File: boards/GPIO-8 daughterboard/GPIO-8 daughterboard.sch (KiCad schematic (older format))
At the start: 1 part, among them P0 HEADER

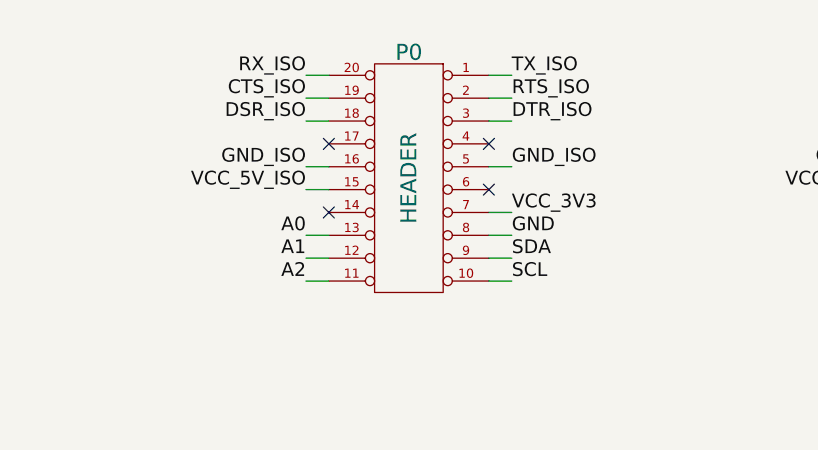
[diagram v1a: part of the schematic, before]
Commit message: Updated daughterboard header pinout in all sheets to be PMOD UART 4/4A compatible
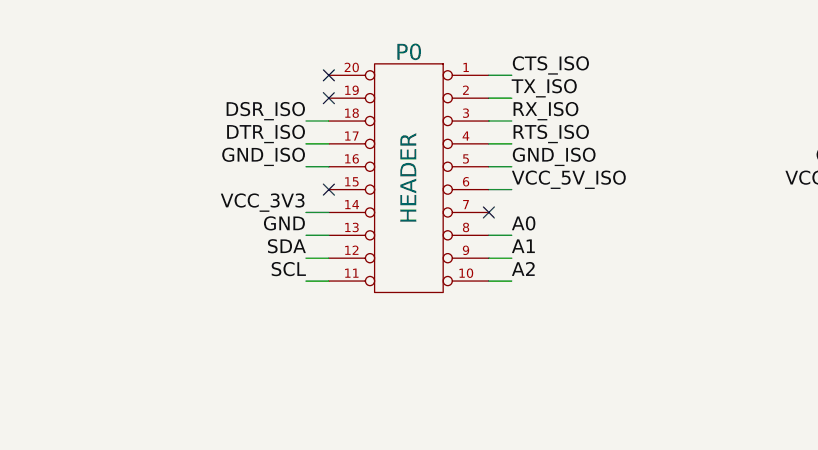
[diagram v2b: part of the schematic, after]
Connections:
- net A0: now also P0.8 (P8); no longer P0.13 (P13)
- net A1: now also P0.9 (P9); no longer P0.12 (P12)
- net A2: now also P0.10 (P10); no longer P0.11 (P11)
- net CTS_ISO: now also P0.1 (P1); no longer P0.19 (P19)
- net DTR_ISO: now also P0.17 (P17); no longer P0.3 (P3)
- net GND: now also P0.13 (P13); no longer P0.8 (P8)
- net RTS_ISO: now also P0.4 (P4); no longer P0.2 (P2)
- net RX_ISO: now also P0.3 (P3); no longer P0.20 (P20)
- net SCL: now also P0.11 (P11); no longer P0.10 (P10)
- net SDA: now also P0.12 (P12); no longer P0.9 (P9)
- net TX_ISO: now also P0.2 (P2); no longer P0.1 (P1)
- net VCC_3V3: now also P0.14 (P14); no longer P0.7 (P7)
- net VCC_5V_ISO: now also P0.6 (P6); no longer P0.15 (P15)
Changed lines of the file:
@@
 Sheet 1 3
 Title ""
-Date "26 jun 2014"
+Date "1 jul 2014"
 Rev ""
 Comp ""
@@
 $EndSheet
 Wire Wire Line
-	3750 3250 3650 3250
+	3750 3450 3650 3450
 Wire Wire Line
-	3750 3350 3650 3350
-Wire Wire Line
-	3750 3450 3650 3450
+	3750 3550 3650 3550
 Wire Wire Line
 	3750 3650 3650 3650
 Wire Wire Line
-	3750 3750 3650 3750
+	4450 3750 4550 3750
 Wire Wire Line
-	3750 3950 3650 3950
+	4450 3950 4550 3950
 Wire Wire Line
 	4550 3250 4450 3250
@@
 	4550 3650 4450 3650
 Wire Wire Line
-	4550 3850 4450 3850
+	3650 3850 3750 3850
 Wire Wire Line
-	4550 3950 4450 3950
+	3650 3950 3750 3950
 Wire Wire Line
-	3750 4050 3650 4050
+	4450 4050 4550 4050
 Wire Wire Line
-	3750 4150 3650 4150
+	4450 4150 4550 4150
 Wire Wire Line
-	4550 4050 4450 4050
+	3650 4050 3750 4050
 Wire Wire Line
-	4550 4150 4450 4150
+	3650 4150 3750 4150
 Text Label 4550 3250 0    60   ~ 0
+CTS_ISO
+Text Label 4550 3350 0    60   ~ 0
 TX_ISO
-Text Label 4550 3350 0    60   ~ 0
-RTS_ISO
 Text Label 4550 3450 0    60   ~ 0
-DTR_ISO
-Text Label 4550 3850 0    60   ~ 0
+RX_ISO
+Text Label 3650 3850 2    60   ~ 0
 VCC_3V3
+Text Label 3650 3950 2    60   ~ 0
+GND
+Text Label 3650 4050 2    60   ~ 0
+SDA
+Text Label 3650 4150 2    60   ~ 0
+SCL
+Text Label 4550 4150 0    60   ~ 0
+A2
+Text Label 4550 4050 0    60   ~ 0
+A1
 Text Label 4550 3950 0    60   ~ 0
-GND
-Text Label 4550 4050 0    60   ~ 0
-SDA
-Text Label 4550 4150 0    60   ~ 0
-SCL
-Text Label 3650 4150 2    60   ~ 0
-A2
-Text Label 3650 4050 2    60   ~ 0
-A1
-Text Label 3650 3950 2    60   ~ 0
 A0
-Text Label 3650 3750 2    60   ~ 0
+Text Label 4550 3750 0    60   ~ 0
 VCC_5V_ISO
 Text Label 3650 3650 2    60   ~ 0
 GND_ISO
+Text Label 3650 3550 2    60   ~ 0
+DTR_ISO
 Text Label 3650 3450 2    60   ~ 0
 DSR_ISO
-Text Label 3650 3350 2    60   ~ 0
-CTS_ISO
-Text Label 3650 3250 2    60   ~ 0
-RX_ISO
 Text Label 4550 3650 0    60   ~ 0
 GND_ISO
-NoConn ~ 4450 3750
-NoConn ~ 4450 3550
-NoConn ~ 3750 3550
-NoConn ~ 3750 3850
 Wire Wire Line
 	6400 3250 6250 3250
@@
 Text Notes 950  7350 0    60   ~ 0
 This sheet abstracts the daughterboard circuits into a hierarchical sheet \nso that they can be integrated into serial expansion motherboard schematic (and PCB) if needed
+Wire Wire Line
+	4450 3550 4550 3550
+Text Label 4550 3550 0    60   ~ 0
+RTS_ISO
+NoConn ~ 3750 3750
+NoConn ~ 4450 3850
+NoConn ~ 3750 3350
+NoConn ~ 3750 3250
 $EndSCHEMATC

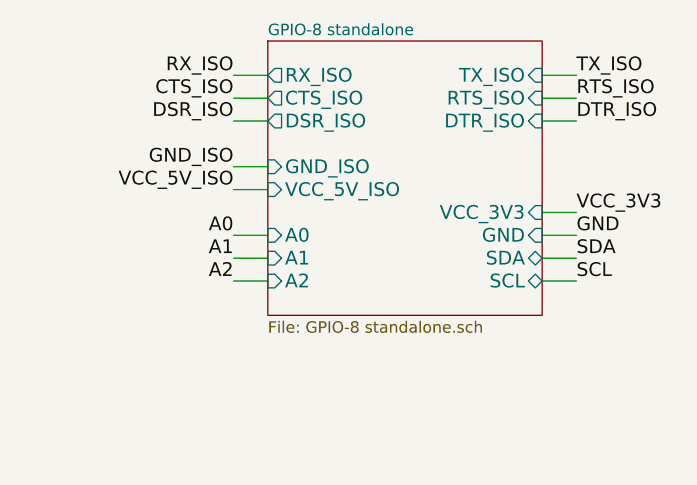
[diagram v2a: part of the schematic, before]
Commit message: Updated GPIO8 dboard to use RS232 adapter block; Changed power hierarchy pin in RS232_adapter_block and PIC-GPIO8 sheets as passive type
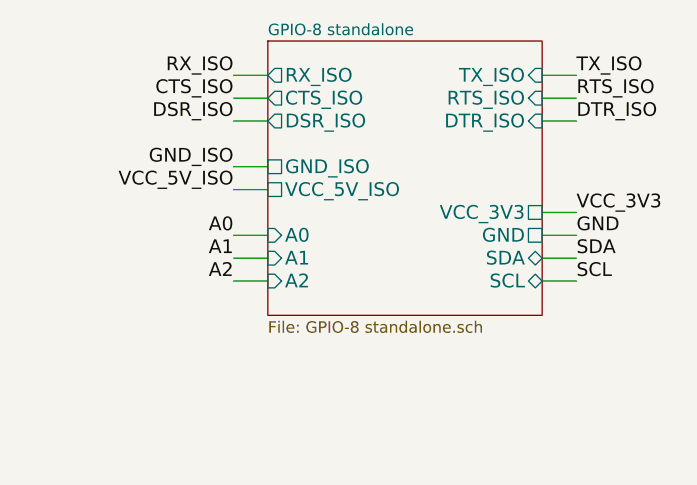
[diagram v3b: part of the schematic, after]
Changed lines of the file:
@@
 $Descr A4 11693 8268
 encoding utf-8
-Sheet 1 3
+Sheet 1 4
 Title ""
 Date "1 jul 2014"
@@
 F6 "DTR_ISO" I R 7600 3450 60
 F7 "DSR_ISO" O L 6400 3450 60
-F8 "VCC_3V3" I R 7600 3850 60
-F9 "GND" I R 7600 3950 60
-F10 "VCC_5V_ISO" I L 6400 3750 60
-F11 "GND_ISO" I L 6400 3650 60
+F8 "VCC_3V3" U R 7600 3850 60
+F9 "GND" U R 7600 3950 60
+F10 "VCC_5V_ISO" U L 6400 3750 60
+F11 "GND_ISO" U L 6400 3650 60
 F12 "SDA" B R 7600 4050 60
 F13 "SCL" B R 7600 4150 60

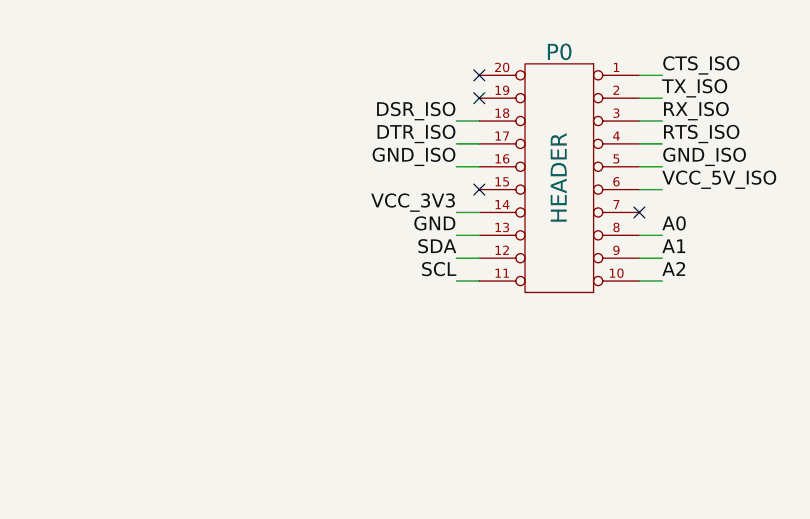
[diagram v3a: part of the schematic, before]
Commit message: Rearranged EEPROM pins in dboard slot pinout to be compatible with PMOD I2C interface
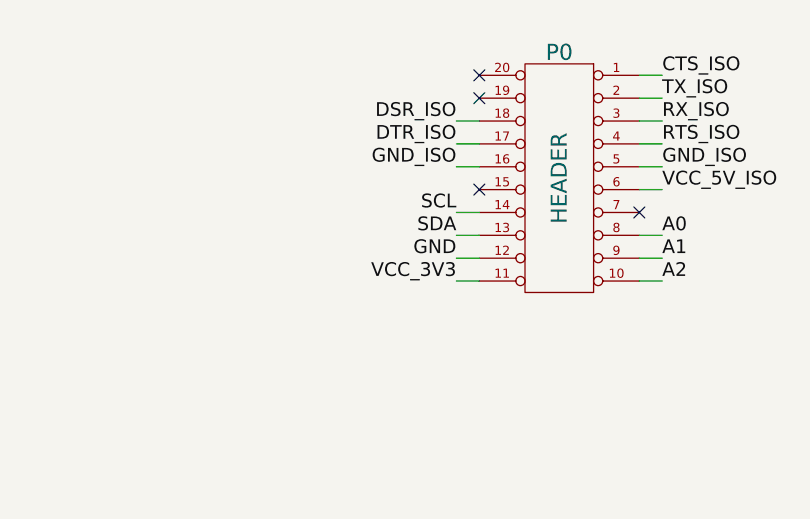
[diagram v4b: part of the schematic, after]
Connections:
- net GND: now also P0.12 (P12); no longer P0.13 (P13)
- net SCL: now also P0.14 (P14); no longer P0.11 (P11)
- net SDA: now also P0.13 (P13); no longer P0.12 (P12)
- net VCC_3V3: now also P0.11 (P11); no longer P0.14 (P14)
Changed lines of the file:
@@
 Sheet 1 4
 Title ""
-Date "1 jul 2014"
+Date "2 jul 2014"
 Rev ""
 Comp ""
@@
 	4550 3650 4450 3650
 Wire Wire Line
-	3650 3850 3750 3850
+	3650 4150 3750 4150
 Wire Wire Line
-	3650 3950 3750 3950
+	3650 4050 3750 4050
 Wire Wire Line
 	4450 4050 4550 4050
@@
 	4450 4150 4550 4150
 Wire Wire Line
-	3650 4050 3750 4050
+	3650 3950 3750 3950
 Wire Wire Line
-	3650 4150 3750 4150
+	3650 3850 3750 3850
 Text Label 4550 3250 0    60   ~ 0
 CTS_ISO
@@
 Text Label 4550 3450 0    60   ~ 0
 RX_ISO
+Text Label 3650 4150 2    60   ~ 0
+VCC_3V3
+Text Label 3650 4050 2    60   ~ 0
+GND
+Text Label 3650 3950 2    60   ~ 0
+SDA
 Text Label 3650 3850 2    60   ~ 0
-VCC_3V3
-Text Label 3650 3950 2    60   ~ 0
-GND
-Text Label 3650 4050 2    60   ~ 0
-SDA
-Text Label 3650 4150 2    60   ~ 0
 SCL
 Text Label 4550 4150 0    60   ~ 0
